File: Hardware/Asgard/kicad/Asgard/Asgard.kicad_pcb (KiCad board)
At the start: 2 copper layers, 17.8 x 61 mm, 9 parts

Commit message: PCB proposal
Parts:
- removed ABSP, BLUETOOTH, DELTAP: CONN_01X04, Socket_Strips:Socket_Strip_Straight_1x04_Pitch2.54mm
- removed OAT: CONN_01X03, Connect:PINHEAD1-3
- added ABSP1: CONN_01X04, Socket_Strips:Socket_Strip_Straight_1x04_Pitch2.54mm, B.Cu at (54.6, 39.4)
- added BLUETOOTH1: CONN_01X04, Socket_Strips:Socket_Strip_Straight_1x04_Pitch2.54mm, B.Cu at (54.6, 49.5)
- added DELTAP1: CONN_01X04, Socket_Strips:Socket_Strip_Straight_1x04_Pitch2.54mm, B.Cu at (47.0, 39.4)
- added GPIO1: CONN_01X03, Connect:PINHEAD1-3, F.Cu at (46.9, 70.2)
- added OAT1: CONN_01X03, Connect:PINHEAD1-3, B.Cu at (46.8, 63.4)
- R1, R2, R3, R4: footprint Resistors_THT:R_Axial_DIN0204_L3.6mm_D1.6mm_P5.08mm_Horizontal -> Resistors_ThroughHole:R_Axial_DIN0204_L3.6mm_D1.6mm_P1.90mm_Vertical
- moved TEENSYV3.6 58.4 mm to (49.5, 31.8), turned to 0 degrees
- moved R2 22.4 mm to (50.7, 38.9), turned to 90 degrees
- moved R1 7.69 mm to (45.7, 54.6), turned to 0 degrees
- moved R4 6.19 mm to (50.7, 32.2), turned to 270 degrees
- moved R3 5.11 mm to (52.1, 54.6)
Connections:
- TEENSYV3.6 pad 10: Net-(TEENSYV3.6-Pad10) -> (no net)
- TEENSYV3.6 pad 11: Net-(TEENSYV3.6-Pad11) -> (no net)
- TEENSYV3.6 pad 12: Net-(TEENSYV3.6-Pad12) -> (no net)
- TEENSYV3.6 pad 13: Net-(TEENSYV3.6-Pad13) -> (no net)
- TEENSYV3.6 pad 14: Net-(TEENSYV3.6-Pad14) -> (no net)
- TEENSYV3.6 pad 15: Net-(TEENSYV3.6-Pad15) -> (no net)
- TEENSYV3.6 pad 16: Net-(TEENSYV3.6-Pad16) -> (no net)
- TEENSYV3.6 pad 17: Net-(TEENSYV3.6-Pad17) -> (no net)
- TEENSYV3.6 pad 18: Net-(TEENSYV3.6-Pad18) -> (no net)
- TEENSYV3.6 pad 19: Net-(TEENSYV3.6-Pad19) -> (no net)
- TEENSYV3.6 pad 20: Net-(TEENSYV3.6-Pad20) -> (no net)
- TEENSYV3.6 pad 21: Net-(TEENSYV3.6-Pad21) -> (no net)
- TEENSYV3.6 pad 22: Net-(TEENSYV3.6-Pad22) -> (no net)
- TEENSYV3.6 pad 23: Net-(TEENSYV3.6-Pad23) -> (no net)
- TEENSYV3.6 pad 24: Net-(TEENSYV3.6-Pad24) -> (no net)
- TEENSYV3.6 pad 25: Net-(TEENSYV3.6-Pad25) -> (no net)
- TEENSYV3.6 pad 26: Net-(TEENSYV3.6-Pad26) -> (no net)
- TEENSYV3.6 pad 28: Net-(TEENSYV3.6-Pad28) -> (no net)
- TEENSYV3.6 pad 29: Net-(TEENSYV3.6-Pad29) -> (no net)
- TEENSYV3.6 pad 30: Net-(TEENSYV3.6-Pad30) -> (no net)
- TEENSYV3.6 pad 31: Net-(TEENSYV3.6-Pad31) -> (no net)
- TEENSYV3.6 pad 34: Net-(TEENSYV3.6-Pad34) -> (no net)
- TEENSYV3.6 pad 35: Net-(TEENSYV3.6-Pad35) -> (no net)
- TEENSYV3.6 pad 36: Net-(TEENSYV3.6-Pad36) -> (no net)
- TEENSYV3.6 pad 38: Net-(TEENSYV3.6-Pad38) -> (no net)
- TEENSYV3.6 pad 39: Net-(TEENSYV3.6-Pad39) -> (no net)
- TEENSYV3.6 pad 4: Net-(TEENSYV3.6-Pad4) -> (no net)
- TEENSYV3.6 pad 40: Net-(TEENSYV3.6-Pad40) -> (no net)
- TEENSYV3.6 pad 41: Net-(TEENSYV3.6-Pad41) -> (no net)
- TEENSYV3.6 pad 42: Net-(TEENSYV3.6-Pad42) -> (no net)
- TEENSYV3.6 pad 45: Net-(TEENSYV3.6-Pad45) -> (no net)
- TEENSYV3.6 pad 46: Net-(TEENSYV3.6-Pad46) -> (no net)
- TEENSYV3.6 pad 5: Net-(TEENSYV3.6-Pad5) -> (no net)
- TEENSYV3.6 pad 6: Net-(TEENSYV3.6-Pad6) -> (no net)
- TEENSYV3.6 pad 7: Net-(TEENSYV3.6-Pad7) -> (no net)
- TEENSYV3.6 pad 8: Net-(TEENSYV3.6-Pad8) -> (no net)
- TEENSYV3.6 pad 9: Net-(TEENSYV3.6-Pad9) -> (no net)
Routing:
- net Net-(GPIO1-Pad2): track 0.00 -> 37.8 mm, vias 0 -> 1
- net Net-(GPIO1-Pad1): track 0.00 -> 35.5 mm, vias 0 -> 1
- net Net-(ABSP1-Pad4): track 20.2 -> 54.3 mm, vias 0 -> 2
- net Net-(BLUETOOTH1-Pad2): track 43.6 -> 19.4 mm, vias 0 -> 1
- net Net-(DELTAP1-Pad4): track 46.3 -> 22.5 mm, vias 2 -> 1
- net Net-(BLUETOOTH1-Pad1): track 36.8 -> 19.4 mm
- net +3V3: track 66.8 -> 49.9 mm
- net GND: track 18.8 -> 33.4 mm, vias 0 -> 2
- net Net-(ABSP1-Pad3): track 35.9 -> 48.3 mm, vias 2 -> 0
- net Net-(DELTAP1-Pad3): track 39.6 -> 33.6 mm, vias 3 -> 0
- net Net-(OAT1-Pad2): track 11.3 -> 12.7 mm, vias 1 -> 0
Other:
- net class Default: clearance 0.3 -> 0.2; trace_width 0.4 -> 0.3
- rule trace_clearance: 0.3 -> 0.2
- rule trace_min: 0.4 -> 0.3

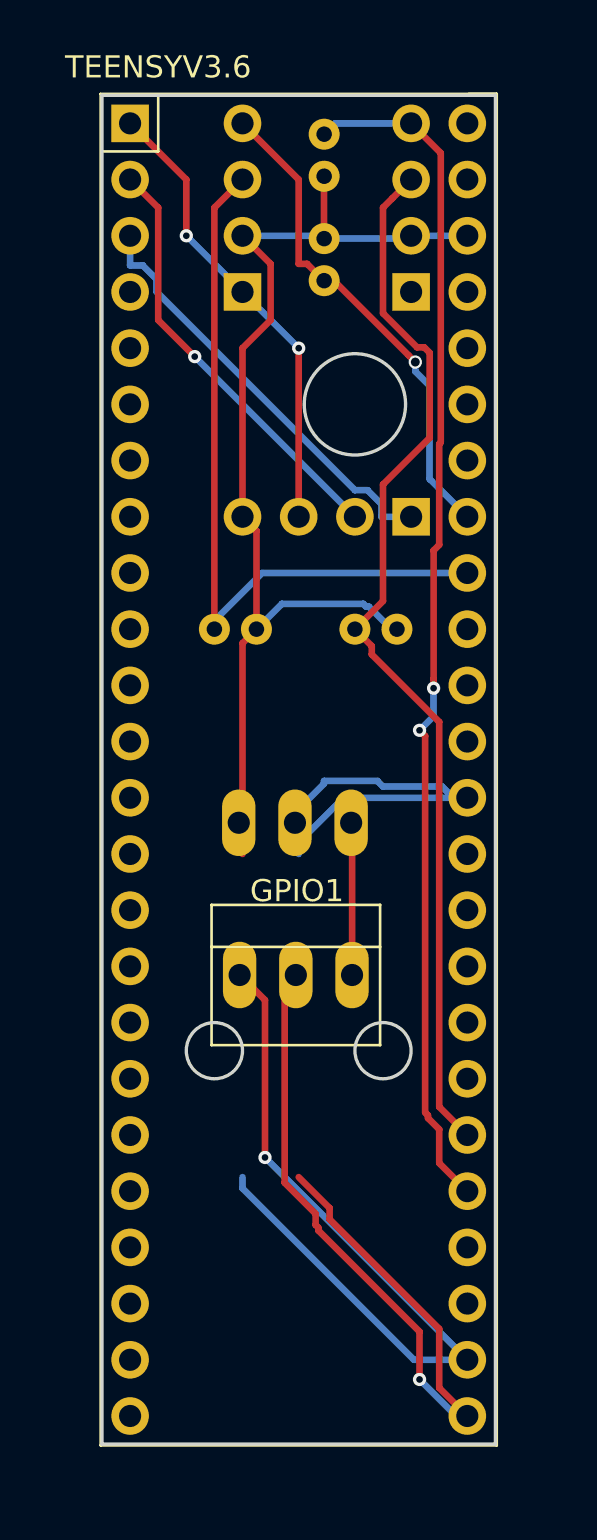
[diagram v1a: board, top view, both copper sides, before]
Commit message: PCB Candidate
Vertical mounted resistors
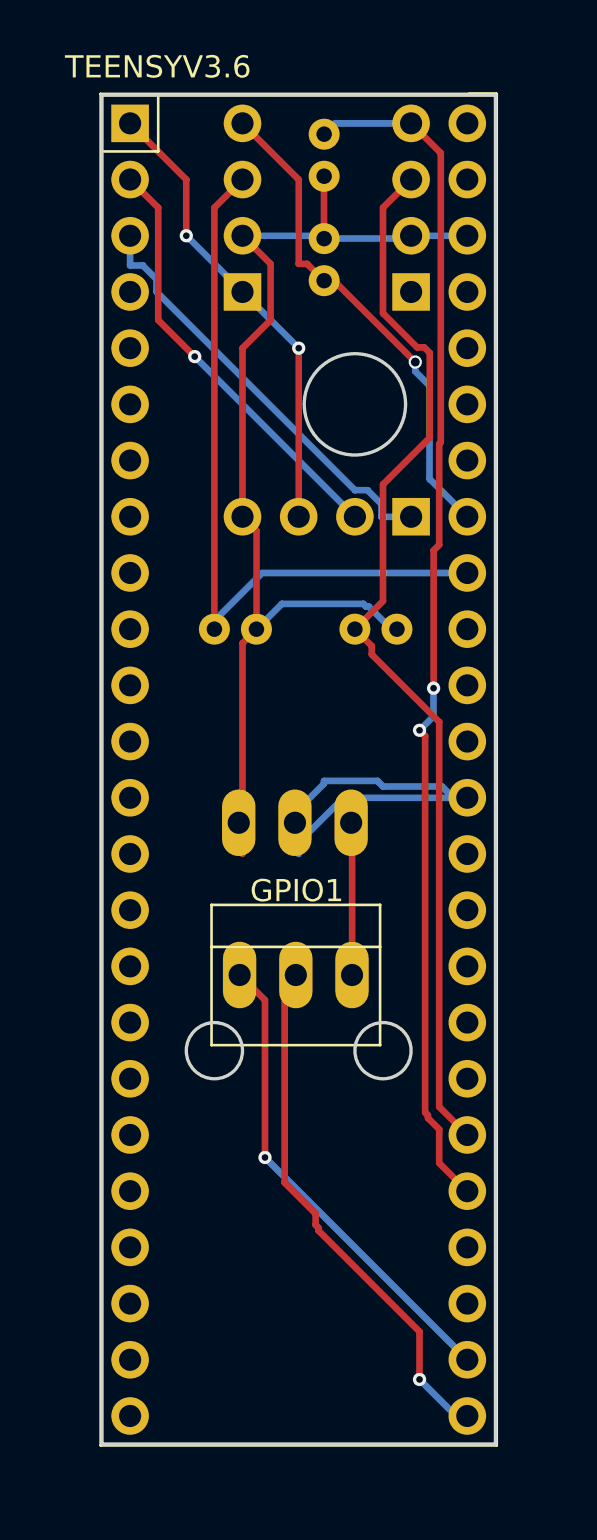
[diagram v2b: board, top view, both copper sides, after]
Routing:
- net Net-(GPIO1-Pad2): track 37.8 -> 23.9 mm
- net Net-(GPIO1-Pad1): track 35.5 -> 21.7 mm

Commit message: PCB Candidate 2
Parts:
- moved TEENSYV3.6 58.4 mm to (49.5, 90.2), turned to 180 degrees
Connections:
- TEENSYV3.6 pad 10: (no net) -> Net-(TEENSYV3.6-Pad10)
- TEENSYV3.6 pad 11: (no net) -> Net-(TEENSYV3.6-Pad11)
- TEENSYV3.6 pad 12: (no net) -> Net-(TEENSYV3.6-Pad12)
- TEENSYV3.6 pad 13: (no net) -> Net-(TEENSYV3.6-Pad13)
- TEENSYV3.6 pad 14: (no net) -> Net-(TEENSYV3.6-Pad14)
- TEENSYV3.6 pad 15: (no net) -> Net-(TEENSYV3.6-Pad15)
- TEENSYV3.6 pad 16: (no net) -> Net-(TEENSYV3.6-Pad16)
- TEENSYV3.6 pad 17: (no net) -> Net-(TEENSYV3.6-Pad17)
- TEENSYV3.6 pad 18: (no net) -> Net-(TEENSYV3.6-Pad18)
- TEENSYV3.6 pad 19: (no net) -> Net-(TEENSYV3.6-Pad19)
- TEENSYV3.6 pad 20: (no net) -> Net-(TEENSYV3.6-Pad20)
- TEENSYV3.6 pad 21: (no net) -> Net-(TEENSYV3.6-Pad21)
- TEENSYV3.6 pad 22: (no net) -> Net-(TEENSYV3.6-Pad22)
- TEENSYV3.6 pad 23: (no net) -> Net-(TEENSYV3.6-Pad23)
- TEENSYV3.6 pad 24: (no net) -> Net-(TEENSYV3.6-Pad24)
- TEENSYV3.6 pad 25: (no net) -> Net-(TEENSYV3.6-Pad25)
- TEENSYV3.6 pad 26: (no net) -> Net-(TEENSYV3.6-Pad26)
- TEENSYV3.6 pad 28: (no net) -> Net-(TEENSYV3.6-Pad28)
- TEENSYV3.6 pad 29: (no net) -> Net-(GPIO1-Pad1)
- TEENSYV3.6 pad 30: (no net) -> Net-(GPIO1-Pad2)
- TEENSYV3.6 pad 31: (no net) -> Net-(TEENSYV3.6-Pad31)
- TEENSYV3.6 pad 34: (no net) -> Net-(TEENSYV3.6-Pad34)
- TEENSYV3.6 pad 35: (no net) -> Net-(TEENSYV3.6-Pad35)
- TEENSYV3.6 pad 36: (no net) -> Net-(TEENSYV3.6-Pad36)
- TEENSYV3.6 pad 38: (no net) -> Net-(TEENSYV3.6-Pad38)
- TEENSYV3.6 pad 39: (no net) -> Net-(TEENSYV3.6-Pad39)
- TEENSYV3.6 pad 4: (no net) -> Net-(TEENSYV3.6-Pad4)
- TEENSYV3.6 pad 40: (no net) -> Net-(TEENSYV3.6-Pad40)
- TEENSYV3.6 pad 41: (no net) -> Net-(TEENSYV3.6-Pad41)
- TEENSYV3.6 pad 42: (no net) -> Net-(TEENSYV3.6-Pad42)
- TEENSYV3.6 pad 45: (no net) -> Net-(TEENSYV3.6-Pad45)
- TEENSYV3.6 pad 46: (no net) -> Net-(TEENSYV3.6-Pad46)
- TEENSYV3.6 pad 47: Net-(GPIO1-Pad1) -> Net-(TEENSYV3.6-Pad47)
- TEENSYV3.6 pad 48: Net-(GPIO1-Pad2) -> Net-(TEENSYV3.6-Pad48)
- TEENSYV3.6 pad 5: (no net) -> Net-(TEENSYV3.6-Pad5)
- TEENSYV3.6 pad 6: (no net) -> Net-(TEENSYV3.6-Pad6)
- TEENSYV3.6 pad 7: (no net) -> Net-(TEENSYV3.6-Pad7)
- TEENSYV3.6 pad 8: (no net) -> Net-(TEENSYV3.6-Pad8)
- TEENSYV3.6 pad 9: (no net) -> Net-(TEENSYV3.6-Pad9)
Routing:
- net Net-(ABSP1-Pad4): track 54.3 -> 19.2 mm, vias 2 -> 1
- net GND: track 33.4 -> 63.3 mm, vias 2 -> 1
- net Net-(DELTAP1-Pad4): track 22.5 -> 50.7 mm, vias 1 -> 5
- net Net-(BLUETOOTH1-Pad2): track 19.4 -> 41.4 mm, vias 1 -> 3
- net +3V3: track 49.9 -> 70.9 mm
- net Net-(BLUETOOTH1-Pad1): track 19.4 -> 36.7 mm, vias 0 -> 3
- net Net-(ABSP1-Pad3): track 48.3 -> 35.1 mm, vias 0 -> 3
- net Net-(GPIO1-Pad2): track 23.9 -> 10.8 mm, vias 1 -> 0
- net Net-(GPIO1-Pad1): track 21.7 -> 11.8 mm, vias 1 -> 0
- net Net-(DELTAP1-Pad3): track 33.6 -> 37.7 mm
- net Net-(OAT1-Pad2): track 12.7 -> 9.36 mm

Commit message: PCB Candidate 3
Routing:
- net Net-(GPIO1-Pad2): track 10.8 -> 12.7 mm
- net GND: track 63.3 -> 64.5 mm
- net Net-(BLUETOOTH1-Pad2): track 41.4 -> 42.6 mm
- net Net-(BLUETOOTH1-Pad1): track 36.7 -> 37.2 mm

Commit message: PCB candidate 4
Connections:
- GPIO1 pad 3: GND -> Net-(GPIO1-Pad3)
- TEENSYV3.6 pad 28: Net-(TEENSYV3.6-Pad28) -> Net-(GPIO1-Pad1)
- TEENSYV3.6 pad 29: Net-(GPIO1-Pad1) -> Net-(GPIO1-Pad2)
- TEENSYV3.6 pad 30: Net-(GPIO1-Pad2) -> Net-(GPIO1-Pad3)
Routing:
- net GND: track 64.5 -> 29.0 mm, vias 1 -> 0
- net Net-(GPIO1-Pad3): track 0.00 -> 13.3 mm
- net Net-(DELTAP1-Pad4): track 50.7 -> 46.9 mm, vias 5 -> 3
- net Net-(ABSP1-Pad3): track 35.1 -> 37.6 mm
- net Net-(GPIO1-Pad1): track 12.1 -> 14.4 mm
- net Net-(GPIO1-Pad2): track 12.7 -> 14.1 mm, vias 0 -> 1
- net Net-(BLUETOOTH1-Pad2): track 42.6 -> 41.4 mm, vias 3 -> 1
- net Net-(BLUETOOTH1-Pad1): track 37.2 -> 36.6 mm, vias 3 -> 0

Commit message: PCB Candidate 5
Added labels on silkboard
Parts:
- GPIO1: moved to B.Cu
- moved OAT1 3.67 mm to (47.0, 59.7)
- moved GPIO1 2.93 mm to (47.0, 67.3)
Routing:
- net GND: track 29.0 -> 0.00 mm
- net Net-(GPIO1-Pad1): track 14.4 -> 17.3 mm
- net Net-(GPIO1-Pad3): track 13.3 -> 16.3 mm
- net Net-(GPIO1-Pad2): track 14.1 -> 16.8 mm
- net Net-(BLUETOOTH1-Pad2): track 41.4 -> 40.2 mm
- net Net-(ABSP1-Pad3): track 37.6 -> 37.2 mm, vias 3 -> 2
- net Net-(DELTAP1-Pad4): vias 3 -> 4
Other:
- board text added: "3.3V"
- board text added: "A0"
- board text added: "A7"
- board text added: "A8"
- board text added: "A9"
- board text added: "ABS"
- board text added: "ADC"
- board text added: "BASICAIRDATA.EU"
- board text added: "BLUETOOTH"
- board text added: "BLUETOOTH OVER THERE"
- board text added: "DELTAP"
- board text added: "GPIO"
- board text added: "OAT"
- board text added: "SENSOR PORTS THIS SIDE"
- board text added: "TEENSY USB SIDE"
- board text removed: "S"
- board text removed: "TEENSY SIDE"
- board text removed: "VCC"

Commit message: PCB Candidate 6
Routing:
- net Net-(ABSP1-Pad3): track 37.2 -> 43.5 mm
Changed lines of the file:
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@@
     (thickness 1.6)
     (drawings 59)
-    (tracks 132)
+    (tracks 145)
     (zones 0)
     (modules 10)
@@
   (gr_circle (center 41.91 90.17) (end 42.41 90.17) (layer Dwgs.User) (width 0.1))
   (gr_circle (center 57.15 90.17) (end 57.65 90.17) (layer Dwgs.User) (width 0.1))
+  (segment (start 48.690012 39.910001) (end 51.184001 39.910001) (width 0.3) (layer F.Cu) (net 1))
+  (segment (start 48.690012 40.707112) (end 48.690012 39.910001) (width 0.3) (layer F.Cu) (net 1))
+  (segment (start 48.953999 50.730001) (end 48.329999 50.106001) (width 0.3) (layer F.Cu) (net 1))
+  (segment (start 52.07 54.61) (end 52.832 53.848) (width 0.3) (layer F.Cu) (net 1))
+  (segment (start 52.832 53.848) (end 52.832 53.467) (width 0.3) (layer F.Cu) (net 1))
+  (segment (start 52.832 53.467) (end 50.095001 50.730001) (width 0.3) (layer F.Cu) (net 1))
+  (segment (start 48.329999 48.953999) (end 48.35144 48.932558) (width 0.3) (layer F.Cu) (net 1))
+  (segment (start 50.095001 50.730001) (end 48.953999 50.730001) (width 0.3) (layer F.Cu) (net 1))
+  (segment (start 51.184001 39.910001) (end 51.730001 39.364001) (width 0.3) (layer F.Cu) (net 1))
+  (segment (start 51.284002 37.91) (end 51.730001 37.464001) (width 0.3) (layer F.Cu) (net 1))
+  (segment (start 48.329999 50.106001) (end 48.329999 48.953999) (width 0.3) (layer F.Cu) (net 1))
+  (segment (start 48.35144 48.932558) (end 48.35144 41.045684) (width 0.3) (layer F.Cu) (net 1))
+  (segment (start 48.35144 41.045684) (end 48.690012 40.707112) (width 0.3) (layer F.Cu) (net 1))
+  (segment (start 51.730001 37.169999) (end 54.61 34.29) (width 0.3) (layer F.Cu) (net 1))
+  (segment (start 51.730001 39.364001) (end 51.730001 38.355999) (width 0.3) (layer F.Cu) (net 1))
+  (segment (start 51.730001 38.355999) (end 51.284002 37.91) (width 0.3) (layer F.Cu) (net 1))
+  (segment (start 51.730001 37.464001) (end 51.730001 37.169999) (width 0.3) (layer F.Cu) (net 1))
   (segment (start 52.07 54.61) (end 50.038 52.578) (width 0.3) (layer F.Cu) (net 1) (status 80000))
   (via (at 50.038 52.578) (size 0.6) (layers F.Cu B.Cu) (net 1) (status 80000))
@@
   (segment (start 43.18 48.26) (end 43.18 45.72) (width 0.3) (layer F.Cu) (net 1) (status 80000))
   (segment (start 43.18 45.72) (end 41.91 44.45) (width 0.3) (layer F.Cu) (net 1) (status 80000))
-  (segment (start 52.07 54.61) (end 52.832 53.848) (width 0.3) (layer F.Cu) (net 1) (status 80000))
-  (segment (start 52.832 53.848) (end 52.832 53.467) (width 0.3) (layer F.Cu) (net 1) (status 80000))
-  (segment (start 52.832 53.467) (end 53.34 52.959) (width 0.3) (layer F.Cu) (net 1) (status 80000))
-  (segment (start 53.34 52.959) (end 53.34 35.56) (width 0.3) (layer F.Cu) (net 1) (status 80000))
-  (segment (start 53.34 35.56) (end 54.61 34.29) (width 0.3) (layer F.Cu) (net 1) (status 80000))
   (segment (start 50.68 32.24) (end 50.673 32.258) (width 0.3) (layer B.Cu) (net 2) (status 80000))
   (segment (start 50.673 32.258) (end 49.911 33.02) (width 0.3) (layer B.Cu) (net 2) (status 80000))
@@
   (segment (start 45.847 57.785) (end 43.942 59.69) (width 0.3) (layer B.Cu) (net 5) (status 80000))
   (segment (start 43.942 59.69) (end 41.91 59.69) (width 0.3) (layer B.Cu) (net 5) (status 80000))
+  (segment (start 46.99 48.327919) (end 46.99 49.53) (width 0.3) (layer F.Cu) (net 7))
+  (segment (start 48.190001 40.500001) (end 46.99 41.700002) (width 0.3) (layer F.Cu) (net 7))
+  (segment (start 46.99 36.83) (end 48.190001 38.030001) (width 0.3) (layer F.Cu) (net 7))
+  (segment (start 46.99 41.700002) (end 46.99 48.327919) (width 0.3) (layer F.Cu) (net 7))
+  (segment (start 48.190001 38.030001) (end 48.190001 40.500001) (width 0.3) (layer F.Cu) (net 7))
   (segment (start 46.99 59.69) (end 48.133 60.833) (width 0.3) (layer F.Cu) (net 7))
   (segment (start 43.18 83.82) (end 41.91 85.09) (width 0.3) (layer F.Cu) (net 7))
@@
   (segment (start 43.815 81.534) (end 43.688 81.661) (width 0.3) (layer F.Cu) (net 7))
   (segment (start 43.688 81.661) (end 43.688 81.788) (width 0.3) (layer F.Cu) (net 7))
-  (segment (start 46.99 36.83) (end 48.26 38.1) (width 0.3) (layer F.Cu) (net 7) (status 80000))
-  (segment (start 48.26 38.1) (end 48.26 40.64) (width 0.3) (layer F.Cu) (net 7) (status 80000))
-  (segment (start 48.26 40.64) (end 46.99 41.91) (width 0.3) (layer F.Cu) (net 7) (status 80000))
-  (segment (start 46.99 41.91) (end 46.99 49.53) (width 0.3) (layer F.Cu) (net 7) (status 80000))
   (segment (start 46.99 49.53) (end 47.625 50.165) (width 0.3) (layer F.Cu) (net 7) (status 80000))
   (segment (start 47.625 50.165) (end 47.625 54.61) (width 0.3) (layer F.Cu) (net 7) (status 80000))
